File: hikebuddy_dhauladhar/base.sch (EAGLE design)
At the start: 112 parts, among them J1 MF-CON-MICROUSB-RIGHT, J2 GPS Port, J5 SOLDER_PAD_2, U1 LTC3586EUFE-1#PBF, U2 MAX17260SETD+, U3 MF-DSC-SOT233-MMBT3904, U4 MF-DSC-SOT233-MMBT3904, U5 DRV2605LTDGSRQ1, U6 BMX160

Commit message: minor tweak
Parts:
- added TP1, TP2: TEST-POINT2, SparkFun-Connectors:TEST-POINT2
- C20: value 1uF -> 0.1uF
- R16: value 10K -> 1K
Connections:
- removed net HAP_EN: ESP32-PICO-D4.IO35, U5.EN
- new net N$19: TP2.1, U1.EN3
- net GND: now also J2.3; no longer J2.1
- net GPS_RESET: now also J2.1; no longer J2.2
- net GPS_SAFEBOOT: now also J2.2; no longer J2.3
- net N$24: now also TP1.1; no longer U1.EN3
- net V_BAT: now also U5.EN
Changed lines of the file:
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@@
 <attribute name="DNP" value="1"/>
 </part>
-<part name="GND9" library="supply1" library_urn="urn:adsk.eagle:library:371" deviceset="GND" device=""/>
 <part name="U1" library="LTC3586EUFE-3_TRPBF" deviceset="LTC3586EUFE-3#TRPBF" device="" package3d_urn="urn:adsk.eagle:package:16348004/2" value=" LTC3586EUFE-1#PBF">
 <attribute name="MP" value="LTC3586EUFE"/>
@@
 <part name="C8" library="SparkFun-Capacitors" deviceset="4.7PF" device="-0603-50V-5%" package3d_urn="urn:adsk.eagle:package:23616/2" value="10uF"/>
 <part name="C38" library="SparkFun-Capacitors" deviceset="4.7PF" device="-0603-50V-5%" package3d_urn="urn:adsk.eagle:package:23616/2" value="10uF"/>
-<part name="R16" library="MF_Passives" deviceset="RESISTOR" device="_0603" package3d_urn="urn:adsk.eagle:package:16347927/2" value="10K"/>
-<part name="C20" library="MF_Passives" deviceset="CAPACITOR_NP" device="_0603" package3d_urn="urn:adsk.eagle:package:16347923/3" value="1uF"/>
+<part name="R16" library="MF_Passives" deviceset="RESISTOR" device="_0603" package3d_urn="urn:adsk.eagle:package:16347927/2" value="1K"/>
+<part name="C20" library="MF_Passives" deviceset="CAPACITOR_NP" device="_0603" package3d_urn="urn:adsk.eagle:package:16347923/3" value="0.1uF"/>
 <part name="U6" library="BMX160" deviceset="BMX160" device=""/>
 <part name="GND23" library="supply1" library_urn="urn:adsk.eagle:library:371" deviceset="GND" device=""/>
@@
 <part name="S1" library="EVQ-P4HB3B" deviceset="EVQ-P4HB3B" device="" override_package3d_urn="urn:adsk.eagle:package:16346036/2" override_package_urn="urn:adsk.eagle:footprint:16346037/1" override_locally_modified="yes"/>
 <part name="SD1" library="MF_Connectors" deviceset="SD_CARD_SLOT" device="_MICRO_RIGHT" package3d_urn="urn:adsk.eagle:package:9948224/2" value="MF-MICROSD"/>
+<part name="GND9" library="supply1" library_urn="urn:adsk.eagle:library:371" deviceset="GND" device=""/>
+<part name="TP1" library="SparkFun-Connectors" deviceset="TEST-POINT" device="2"/>
+<part name="TP2" library="SparkFun-Connectors" deviceset="TEST-POINT" device="2"/>
 </parts>
 <sheets>
@@
 <attribute name="DNP" x="165.1" y="193.04" size="1.778" layer="96" rot="R270" display="off"/>
 </instance>
-<instance part="GND9" gate="1" x="160.02" y="185.42" smashed="yes">
-<attribute name="VALUE" x="157.48" y="182.88" size="1.778" layer="96"/>
-</instance>
 <instance part="U5" gate="G$1" x="226.06" y="38.1" smashed="yes">
 <attribute name="NAME" x="213.36" y="56.88" size="2.0828" layer="95" ratio="10" rot="SR0"/>
@@
 <attribute name="NAME" x="347.98" y="173.99" size="1.016" layer="95" font="vector" align="top-left"/>
 <attribute name="VALUE" x="347.98" y="171.45" size="1.016" layer="96" font="vector"/>
+</instance>
+<instance part="GND9" gate="1" x="165.1" y="185.42" smashed="yes">
+<attribute name="VALUE" x="162.56" y="182.88" size="1.778" layer="96"/>
 </instance>
 </instances>
@@
 </segment>
 <segment>
-<pinref part="J2" gate="G$1" pin="1"/>
-<pinref part="GND9" gate="1" pin="GND"/>
-</segment>
-<segment>
 <pinref part="U5" gate="G$1" pin="IN/TRIG"/>
 <wire x1="208.28" y1="45.72" x2="226.06" y2="45.72" width="0.1524" layer="91"/>
@@
 <junction x="403.86" y="106.68"/>
 </segment>
+<segment>
+<pinref part="J2" gate="G$1" pin="3"/>
+<pinref part="GND9" gate="1" pin="GND"/>
+</segment>
 </net>
 <net name="N$1" class="0">
@@
 <net name="GPS_RESET" class="0">
 <segment>
+<pinref part="J2" gate="G$1" pin="1"/>
+<label x="160.02" y="187.96" size="1.27" layer="95" rot="R270" xref="yes"/>
 <pinref part="R18" gate="G$1" pin="2"/>
-<wire x1="175.26" y1="170.18" x2="162.56" y2="170.18" width="0.1524" layer="91"/>
-<pinref part="J2" gate="G$1" pin="2"/>
-<wire x1="162.56" y1="170.18" x2="162.56" y2="187.96" width="0.1524" layer="91"/>
-<label x="162.56" y="187.96" size="1.27" layer="95" rot="R270" xref="yes"/>
+<wire x1="175.26" y1="170.18" x2="160.02" y2="170.18" width="0.1524" layer="91"/>
+<wire x1="160.02" y1="187.96" x2="160.02" y2="170.18" width="0.1524" layer="91"/>
 </segment>
 </net>
@@
 <segment>
 <pinref part="R19" gate="G$1" pin="2"/>
-<wire x1="175.26" y1="162.56" x2="165.1" y2="162.56" width="0.1524" layer="91"/>
-<pinref part="J2" gate="G$1" pin="3"/>
-<wire x1="165.1" y1="187.96" x2="165.1" y2="162.56" width="0.1524" layer="91"/>
-<label x="165.1" y="187.96" size="1.27" layer="95" rot="R270" xref="yes"/>
+<wire x1="175.26" y1="162.56" x2="162.56" y2="162.56" width="0.1524" layer="91"/>
+<pinref part="J2" gate="G$1" pin="2"/>
+<wire x1="162.56" y1="187.96" x2="162.56" y2="162.56" width="0.1524" layer="91"/>
+<label x="162.56" y="187.96" size="1.27" layer="95" rot="R270" xref="yes"/>
 </segment>
 </net>
@@
 </segment>
 </net>
-<net name="HAP_EN" class="0">
-<segment>
-<pinref part="U5" gate="G$1" pin="EN"/>
-<wire x1="208.28" y1="38.1" x2="205.74" y2="38.1" width="0.1524" layer="91"/>
-<label x="205.74" y="38.1" size="1.27" layer="95" rot="R180" xref="yes"/>
-</segment>
-<segment>
-<pinref part="ESP32-PICO-D4" gate="G$1" pin="IO35"/>
-<wire x1="30.48" y1="165.1" x2="27.94" y2="165.1" width="0.1524" layer="91"/>
-<label x="27.94" y="165.1" size="1.27" layer="95" rot="R180" xref="yes"/>
-</segment>
-</net>
 <net name="N$50" class="0">
 <segment>
@@
 <pinref part="C37" gate="G$1" pin="2"/>
 <label x="243.84" y="58.42" size="1.27" layer="95" xref="yes"/>
+<pinref part="U5" gate="G$1" pin="EN"/>
+<wire x1="208.28" y1="38.1" x2="203.2" y2="38.1" width="0.1524" layer="91"/>
+<wire x1="203.2" y1="38.1" x2="203.2" y2="53.34" width="0.1524" layer="91"/>
+<wire x1="203.2" y1="53.34" x2="243.84" y2="53.34" width="0.1524" layer="91"/>
 </segment>
 <segment>
@@
 <attribute name="NAME" x="48.26" y="64.516" size="1.016" layer="95" font="vector" rot="R180" align="top-left"/>
 <attribute name="VALUE" x="48.26" y="67.564" size="1.016" layer="96" font="vector" rot="R180"/>
+</instance>
+<instance part="TP1" gate="G$1" x="78.74" y="88.9" smashed="yes">
+<attribute name="NAME" x="76.2" y="91.44" size="1.778" layer="95" font="vector"/>
+<attribute name="VALUE" x="76.2" y="86.36" size="1.778" layer="96" font="vector"/>
+</instance>
+<instance part="TP2" gate="G$1" x="86.36" y="88.9" smashed="yes" rot="R180">
+<attribute name="NAME" x="88.9" y="86.36" size="1.778" layer="95" font="vector" rot="R180"/>
+<attribute name="VALUE" x="88.9" y="91.44" size="1.778" layer="96" font="vector" rot="R180"/>
 </instance>
 </instances>
@@
 <net name="N$24" class="0">
 <segment>
-<pinref part="U1" gate="G$1" pin="EN3"/>
-<wire x1="93.98" y1="88.9" x2="73.66" y2="88.9" width="0.1524" layer="91"/>
-<wire x1="73.66" y1="88.9" x2="73.66" y2="83.82" width="0.1524" layer="91"/>
+<wire x1="78.74" y1="88.9" x2="78.74" y2="83.82" width="0.1524" layer="91"/>
 <pinref part="U1" gate="G$1" pin="FAULT"/>
-<wire x1="73.66" y1="83.82" x2="58.42" y2="83.82" width="0.1524" layer="91"/>
+<wire x1="78.74" y1="83.82" x2="58.42" y2="83.82" width="0.1524" layer="91"/>
 <pinref part="R16" gate="G$1" pin="P$2"/>
 <wire x1="58.42" y1="83.82" x2="53.34" y2="83.82" width="0.1524" layer="91"/>
@@
 <wire x1="53.34" y1="83.82" x2="50.8" y2="83.82" width="0.1524" layer="91"/>
 <junction x="53.34" y="83.82"/>
-</segment>
-</net>
+<pinref part="TP1" gate="G$1" pin="1"/>
+</segment>
+</net>
+<net name="N$19" class="0">
+<segment>
+<pinref part="U1" gate="G$1" pin="EN3"/>
+<pinref part="TP2" gate="G$1" pin="1"/>
+<wire x1="86.36" y1="88.9" x2="93.98" y2="88.9" width="0.1524" layer="91"/>
+</segment>
+</net>

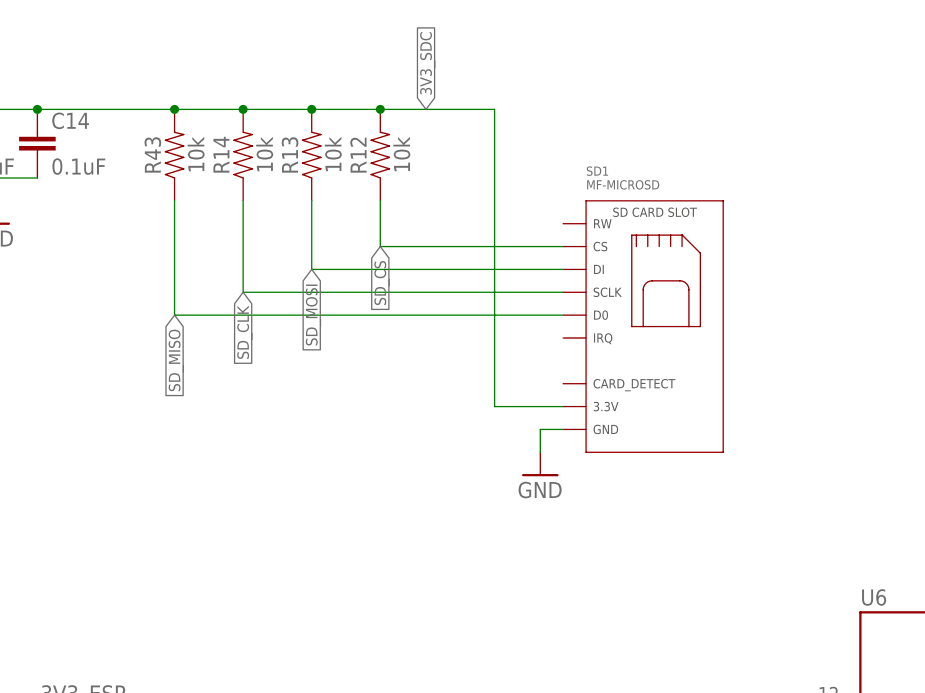
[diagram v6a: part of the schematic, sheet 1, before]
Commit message: changed sd card to Molex, added pcbway acknowledgement
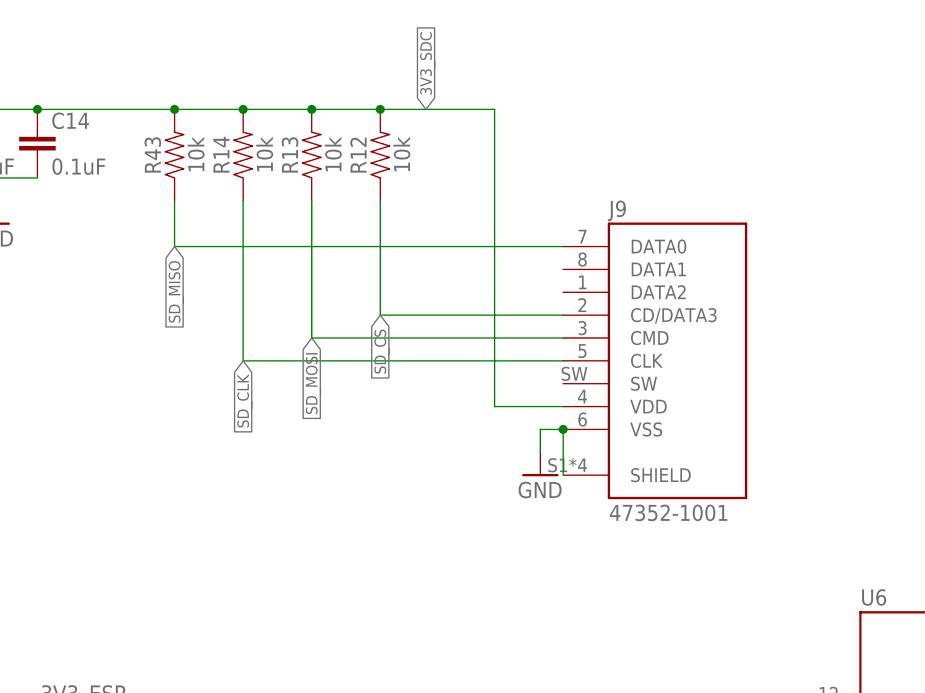
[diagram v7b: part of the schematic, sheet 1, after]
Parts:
- removed SD1: MF-MICROSD, MF_Connectors:SD_CARD_SLOT_MICRO_RIGHT
- added J9: 47352-1001, 47352-1001:47352-1001
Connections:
- net 3V3_SDC: now also J9.VDD; no longer SD1.3.3V
- net GND: now also J9.SHIELD, J9.VSS; no longer SD1.GND
- net SD_CLK: now also J9.CLK; no longer SD1.SCLK
- net SD_CS: now also J9.CD/DATA3; no longer SD1.CS
- net SD_MISO: now also J9.DATA0; no longer SD1.D0
- net SD_MOSI: now also J9.CMD; no longer SD1.DI
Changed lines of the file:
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@@
 <part name="S4" library="EVQ-P4HB3B" deviceset="EVQ-P4HB3B" device="" override_package3d_urn="urn:adsk.eagle:package:16346036/2" override_package_urn="urn:adsk.eagle:footprint:16346037/1" override_locally_modified="yes"/>
 <part name="S1" library="EVQ-P4HB3B" deviceset="EVQ-P4HB3B" device="" override_package3d_urn="urn:adsk.eagle:package:16346036/2" override_package_urn="urn:adsk.eagle:footprint:16346037/1" override_locally_modified="yes"/>
-<part name="SD1" library="MF_Connectors" deviceset="SD_CARD_SLOT" device="_MICRO_RIGHT" package3d_urn="urn:adsk.eagle:package:9948224/2" value="MF-MICROSD"/>
 <part name="GND9" library="supply1" library_urn="urn:adsk.eagle:library:371" deviceset="GND" device=""/>
 <part name="TP1" library="SparkFun-Connectors" deviceset="TEST-POINT" device="2"/>
 <part name="TP2" library="SparkFun-Connectors" deviceset="TEST-POINT" device="2"/>
+<part name="J9" library="47352-1001" deviceset="47352-1001" device="" package3d_urn="urn:adsk.eagle:package:16346114/2"/>
 </parts>
 <sheets>
@@
 <attribute name="VALUE" x="60.94628125" y="15.22628125" size="2.54456875" layer="96"/>
 </instance>
-<instance part="SD1" gate="G$1" x="347.98" y="170.18" smashed="yes">
-<attribute name="NAME" x="347.98" y="173.99" size="1.016" layer="95" font="vector" align="top-left"/>
-<attribute name="VALUE" x="347.98" y="171.45" size="1.016" layer="96" font="vector"/>
-</instance>
 <instance part="GND9" gate="1" x="165.1" y="185.42" smashed="yes">
 <attribute name="VALUE" x="162.56" y="182.88" size="1.778" layer="96"/>
+</instance>
+<instance part="J9" gate="G$1" x="358.14" y="152.4" smashed="yes">
+<attribute name="NAME" x="350.52" y="168.402" size="1.778" layer="95"/>
+<attribute name="VALUE" x="350.52" y="134.62" size="1.778" layer="96"/>
 </instance>
 </instances>
@@
 <wire x1="342.9" y1="144.78" x2="342.9" y2="142.24" width="0.1524" layer="91"/>
 <pinref part="GND12" gate="1" pin="GND"/>
-<pinref part="SD1" gate="G$1" pin="GND"/>
+<pinref part="J9" gate="G$1" pin="VSS"/>
+<pinref part="J9" gate="G$1" pin="SHIELD"/>
+<wire x1="345.44" y1="139.7" x2="345.44" y2="144.78" width="0.1524" layer="91"/>
+<junction x="345.44" y="144.78"/>
 </segment>
 <segment>
@@
 <net name="SD_CS" class="0">
 <segment>
-<wire x1="345.44" y1="165.1" x2="325.12" y2="165.1" width="0.1524" layer="91"/>
+<wire x1="345.44" y1="157.48" x2="325.12" y2="157.48" width="0.1524" layer="91"/>
 <pinref part="R12" gate="G$1" pin="1"/>
-<wire x1="325.12" y1="165.1" x2="325.12" y2="170.18" width="0.1524" layer="91"/>
-<label x="325.12" y="165.1" size="1.27" layer="95" rot="R270" xref="yes"/>
-<pinref part="SD1" gate="G$1" pin="CS"/>
+<wire x1="325.12" y1="157.48" x2="325.12" y2="170.18" width="0.1524" layer="91"/>
+<label x="325.12" y="157.48" size="1.27" layer="95" rot="R270" xref="yes"/>
+<pinref part="J9" gate="G$1" pin="CD/DATA3"/>
 </segment>
 <segment>
@@
 <segment>
 <pinref part="R13" gate="G$1" pin="1"/>
-<wire x1="345.44" y1="162.56" x2="317.5" y2="162.56" width="0.1524" layer="91"/>
-<wire x1="317.5" y1="162.56" x2="317.5" y2="170.18" width="0.1524" layer="91"/>
-<label x="317.5" y="162.56" size="1.27" layer="95" rot="R270" xref="yes"/>
-<pinref part="SD1" gate="G$1" pin="DI"/>
+<wire x1="345.44" y1="154.94" x2="317.5" y2="154.94" width="0.1524" layer="91"/>
+<wire x1="317.5" y1="154.94" x2="317.5" y2="170.18" width="0.1524" layer="91"/>
+<label x="317.5" y="154.94" size="1.27" layer="95" rot="R270" xref="yes"/>
+<pinref part="J9" gate="G$1" pin="CMD"/>
 </segment>
 <segment>
@@
 <segment>
 <pinref part="R14" gate="G$1" pin="1"/>
-<wire x1="345.44" y1="160.02" x2="309.88" y2="160.02" width="0.1524" layer="91"/>
-<wire x1="309.88" y1="160.02" x2="309.88" y2="170.18" width="0.1524" layer="91"/>
-<label x="309.88" y="160.02" size="1.27" layer="95" rot="R270" xref="yes"/>
-<pinref part="SD1" gate="G$1" pin="SCLK"/>
+<wire x1="345.44" y1="152.4" x2="309.88" y2="152.4" width="0.1524" layer="91"/>
+<wire x1="309.88" y1="152.4" x2="309.88" y2="170.18" width="0.1524" layer="91"/>
+<label x="309.88" y="152.4" size="1.27" layer="95" rot="R270" xref="yes"/>
+<pinref part="J9" gate="G$1" pin="CLK"/>
 </segment>
 <segment>
@@
 <net name="SD_MISO" class="0">
 <segment>
-<wire x1="345.44" y1="157.48" x2="302.26" y2="157.48" width="0.1524" layer="91"/>
-<wire x1="302.26" y1="157.48" x2="302.26" y2="170.18" width="0.1524" layer="91"/>
-<label x="302.26" y="157.48" size="1.27" layer="95" rot="R270" xref="yes"/>
+<wire x1="345.44" y1="165.1" x2="302.26" y2="165.1" width="0.1524" layer="91"/>
+<wire x1="302.26" y1="165.1" x2="302.26" y2="170.18" width="0.1524" layer="91"/>
+<label x="302.26" y="165.1" size="1.27" layer="95" rot="R270" xref="yes"/>
 <pinref part="R43" gate="G$1" pin="1"/>
-<pinref part="SD1" gate="G$1" pin="D0"/>
+<pinref part="J9" gate="G$1" pin="DATA0"/>
 </segment>
 <segment>
@@
 <pinref part="R43" gate="G$1" pin="2"/>
 <junction x="302.26" y="180.34"/>
-<pinref part="SD1" gate="G$1" pin="3.3V"/>
-</segment>
-</net>
+<pinref part="J9" gate="G$1" pin="VDD"/>
+</segment>
+</net>
